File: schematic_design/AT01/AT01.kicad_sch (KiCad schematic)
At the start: 42 parts, among them J1 JST Connector, J2 Conn_01x08_Pin, J3 USB_C_Receptacle_USB2.0, M2 Motor_DC (Pump), M3 Motor_DC (Solenoid), Q1 DMG2301L, Q2 2N7002, Q3 2N7002, SW1 SW_Push, U1 MPRLS0025PA00001A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

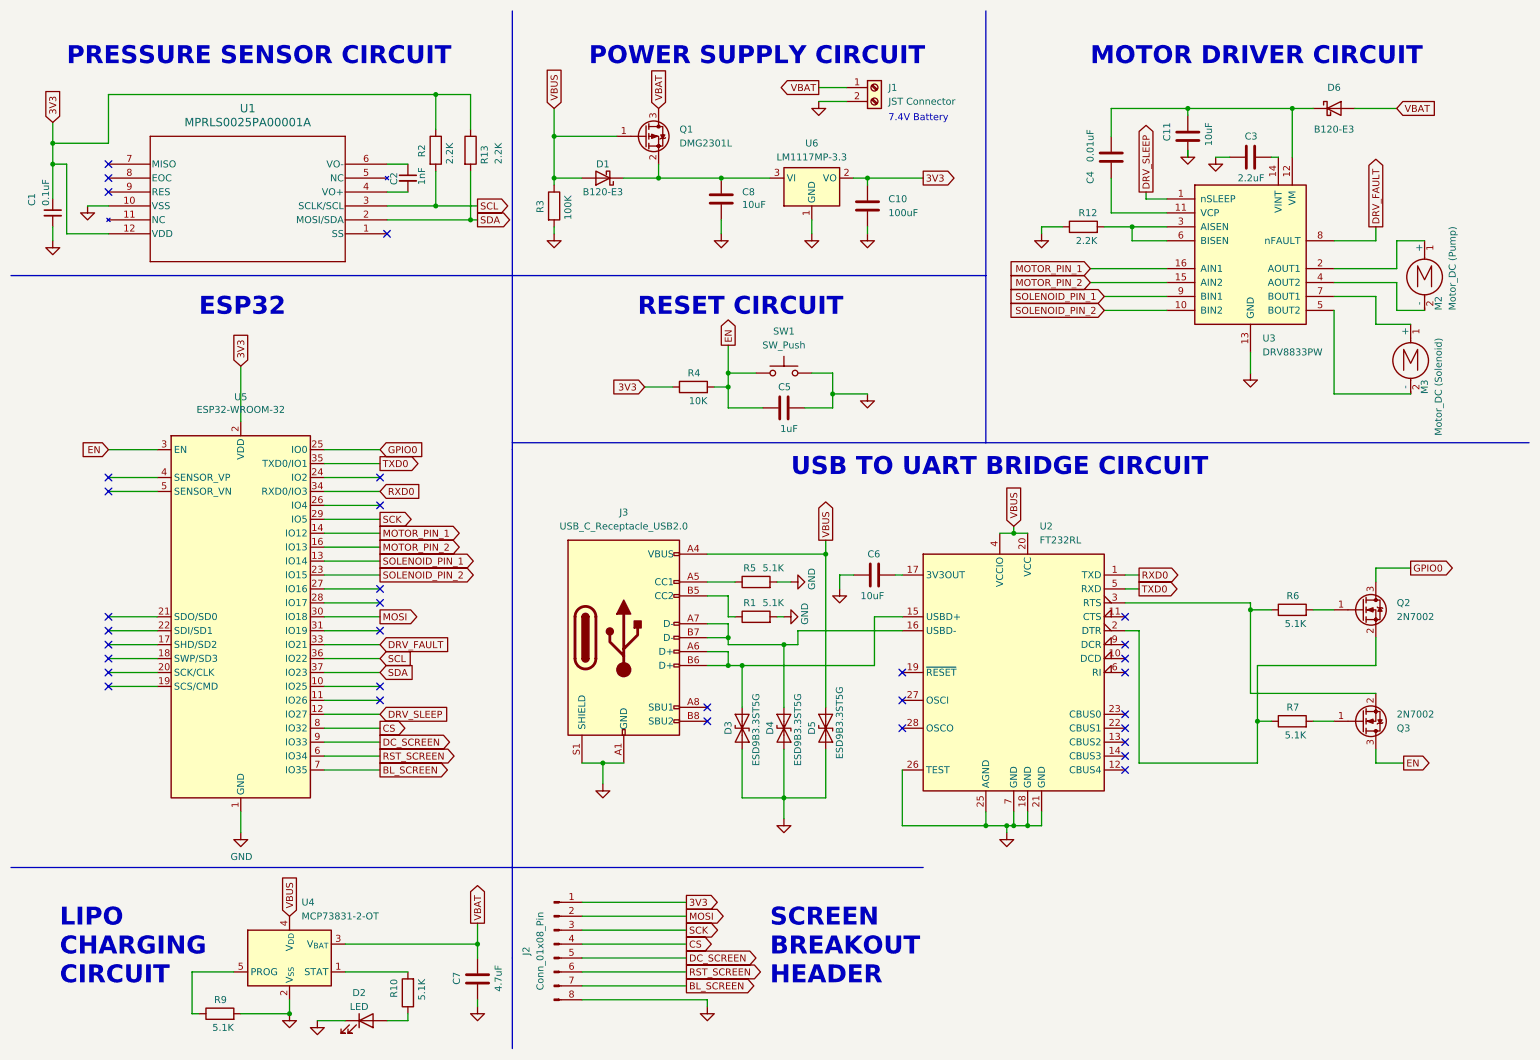
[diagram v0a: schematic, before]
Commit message: reddit fixes, adding buttons/leds, restarting pcb layout
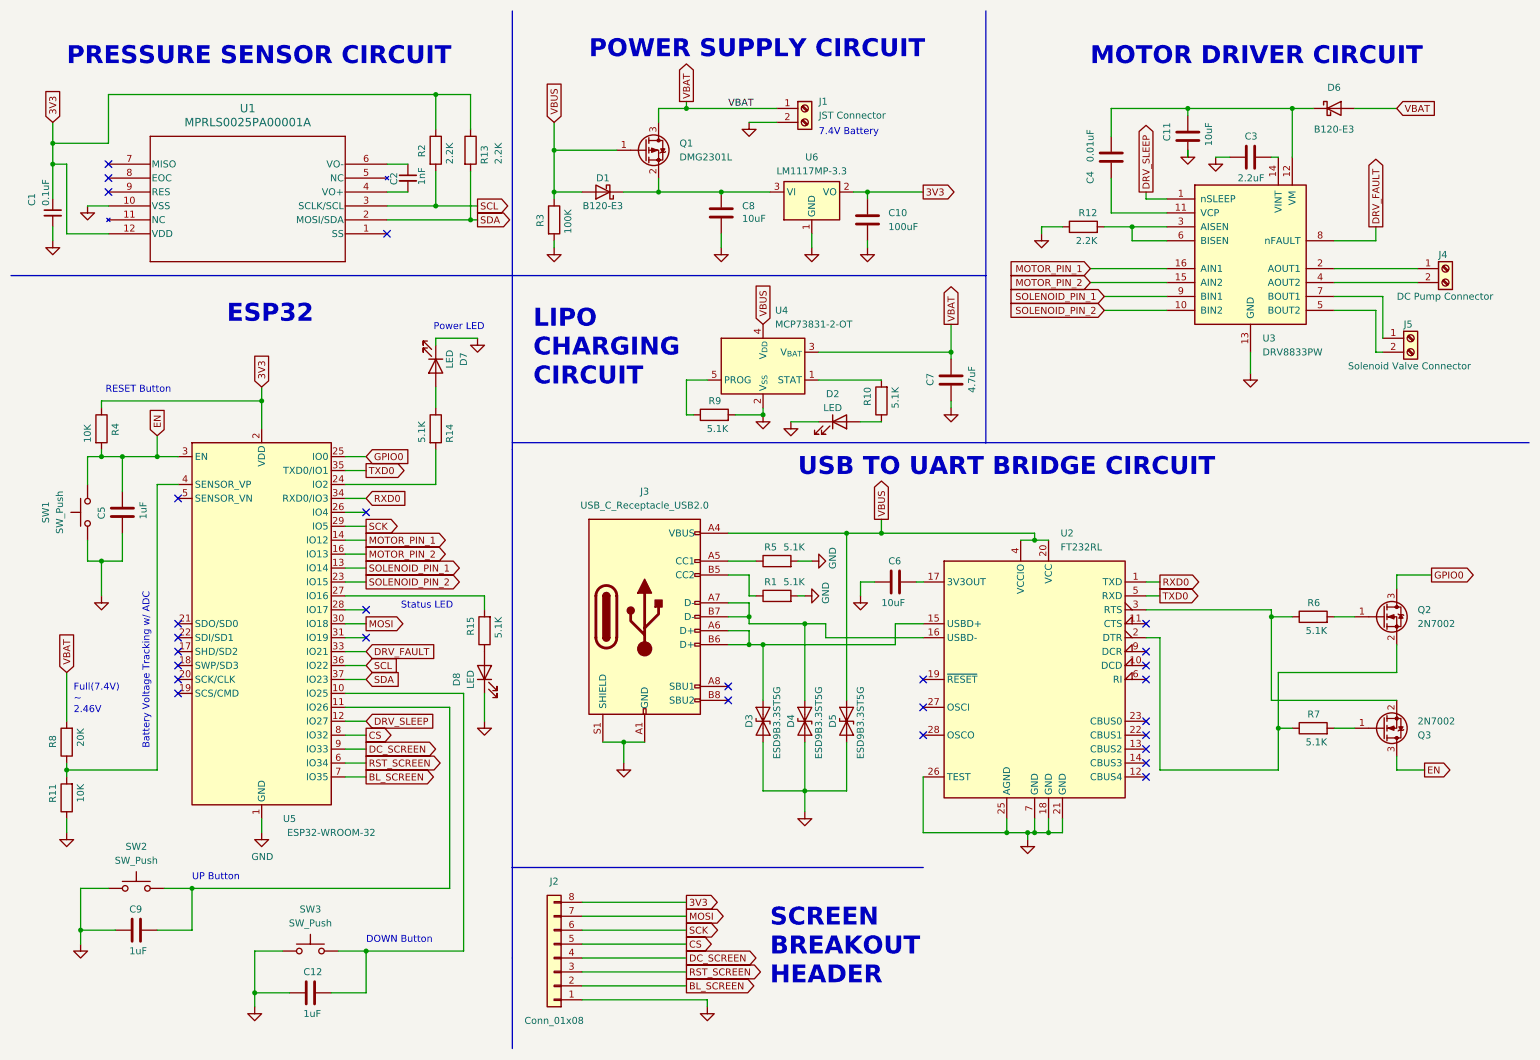
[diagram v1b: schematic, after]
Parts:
- removed J2: Conn_01x08_Pin, Connector_PinHeader_1.00mm:PinHeader_1x08_P1.00mm_Vertical, symbol Connector:Conn_01x08_Pin
- removed M2: Motor_DC (Pump), Connector_Samtec_HPM_THT:Samtec_HPM-02-05-x-S_Straight_1x02_Pitch5.08mm, symbol Motor:Motor_DC
- removed M3: Motor_DC (Solenoid), Connector_Samtec_HPM_THT:Samtec_HPM-02-05-x-S_Straight_1x02_Pitch5.08mm, symbol Motor:Motor_DC
- added C12, C9: 1uF, Capacitor_SMD:C_01005_0402Metric_Pad0.57x0.30mm_HandSolder, symbol Device:C
- added D7, D8: LED, LED_THT:LED_D3.0mm, symbol Device:LED
- added J2: Conn_01x08, Connector_PinHeader_1.00mm:PinHeader_1x08_P1.00mm_Vertical, symbol Connector_Generic:Conn_01x08
- added J4: DC Pump Connector, Connector_JST:JST_EH_S2B-EH_1x02_P2.50mm_Horizontal, symbol Connector:Screw_Terminal_01x02
- added J5: Solenoid Valve Connector, Connector_JST:JST_EH_S2B-EH_1x02_P2.50mm_Horizontal, symbol Connector:Screw_Terminal_01x02
- added R11: 10K, Resistor_SMD:R_0402_1005Metric_Pad0.72x0.64mm_HandSolder, symbol Device:R
- added R14, R15: 5.1K, Resistor_SMD:R_0402_1005Metric_Pad0.72x0.64mm_HandSolder, symbol Device:R
- added R8: 20K, Resistor_SMD:R_0402_1005Metric_Pad0.72x0.64mm_HandSolder, symbol Device:R
- added SW2, SW3: SW_Push, Button_Switch_THT:SW_PUSH_6mm, symbol Switch:SW_Push
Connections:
- net 3V3: now also J2.8 (Pin_8)
- net BL_SCREEN: now also J2.2 (Pin_2)
- net CS: now also J2.5 (Pin_5)
- net DC_SCREEN: now also J2.4 (Pin_4)
- net GND: now also C12.2, C9.2, D7.1 (K), D8.1 (K), J2.1 (Pin_1), R11.1, SW2.2, SW3.2
- net MOSI: now also J2.7 (Pin_7)
- net RST_SCREEN: now also J2.3 (Pin_3)
- net SCK: now also J2.6 (Pin_6)
- net VBAT: now also R8.2
- net at U5.10 (IO25): now also C12.1, SW3.1
- net at U5.11 (IO26): now also C9.1, SW2.1
- net at U5.24 (IO2): now also R14.2
- net at U5.27 (IO16): now also R15.2
- net at U5.4 (SENSOR_VP): now also R11.2, R8.1
- net at U3.2 (AOUT1): now also J4.1 (Pin_1)
- net at U3.4 (AOUT2): now also J4.2 (Pin_2)
- net at U3.5 (BOUT2): now also J5.2 (Pin_2)
- net at U3.7 (BOUT1): now also J5.1 (Pin_1)
- new net: D7.2 (A), R14.1
- new net: D8.2 (A), R15.1
- no-connect marks 33 -> 28
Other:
- note added: "Battery Voltage Tracking w/ ADC"
- note added: "DOWN Button"
- note added: "Full(7.4V) ~ 2.46V"
- note added: "Power LED"
- note added: "RESET Button"
- note added: "Status LED"
- note added: "UP Button"
- note removed: "RESET CIRCUIT"
- title: BP - Initial Revision -> AT01 - Initial Revision
- moved on the sheet: C10, C5, C6, C7, C8, D1, D2, D3, D4, D5, J1, J3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

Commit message: initial layout revision
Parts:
- added C13: 10uF, Capacitor_SMD:C_1206_3216Metric_Pad1.33x1.80mm_HandSolder, symbol Device:C_Polarized_Small_US
- added H1, H2, H3, H4: MountingHole, MountingHole:MountingHole_2.2mm_M2_ISO7380, symbol Mechanical:MountingHole
- C1, C10, C11, C12, C2, C3, C4, C5, C6, C7, C8, C9: footprint Capacitor_SMD:C_01005_0402Metric_Pad0.57x0.30mm_HandSolder -> Capacitor_SMD:C_0402_1005Metric_Pad0.74x0.62mm_HandSolder
- J3: footprint Connector_USB:USB_C_Receptacle_Molex_105450-0101 -> Connector_USB:USB_C_Receptacle_HRO_TYPE-C-31-M-12
- U5: footprint RF_Module:ESP32-WROOM-32D -> RF_Module:ESP32-WROOM-32U; symbol RF_Module:ESP32-WROOM-32D -> RF_Module:ESP32-WROOM-32U
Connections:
- net 3V3: now also C13.1
- net BL_SCREEN: now also J2.3 (Pin_3); no longer J2.2 (Pin_2)
- net CS: now also J2.4 (Pin_4); no longer J2.5 (Pin_5)
- net DC_SCREEN: now also J2.5 (Pin_5); no longer J2.4 (Pin_4)
- net DRV_FAULT: now also U5.12 (IO27); no longer U5.33 (IO21)
- net DRV_SLEEP: now also U5.11 (IO26); no longer U5.12 (IO27)
- net GND: now also C13.2
- net RST_SCREEN: now also J2.2 (Pin_2); no longer J2.3 (Pin_3)
- net at C9.1, SW2.1: now also U5.33 (IO21); no longer U5.11 (IO26)
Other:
- moved on the sheet: C10, C11, R8

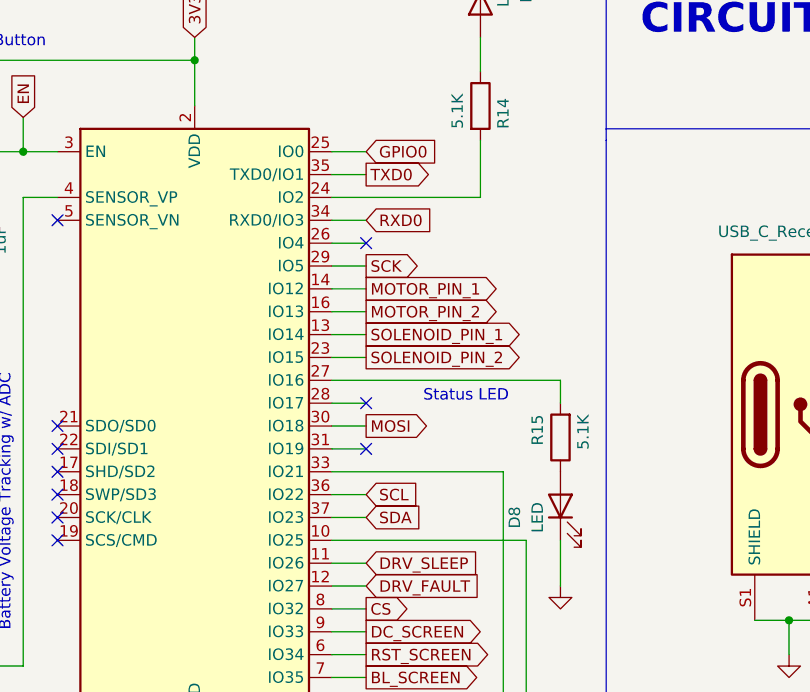
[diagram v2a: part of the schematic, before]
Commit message: updated incorrect UART pins
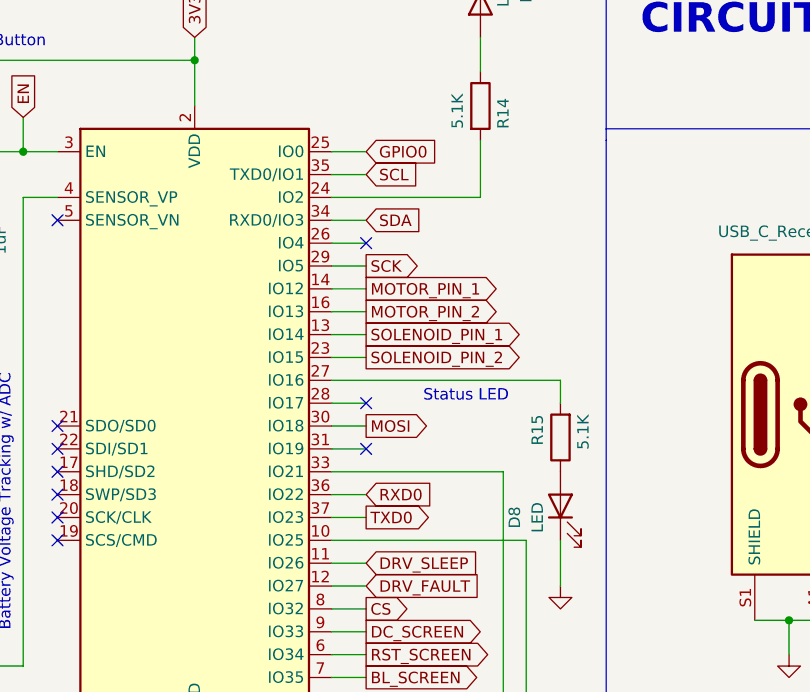
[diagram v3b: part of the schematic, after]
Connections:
- net RXD0: now also U5.36 (IO22); no longer U5.34 (RXD0/IO3)
- net SCL: now also U5.35 (TXD0/IO1); no longer U5.36 (IO22)
- net SDA: now also U5.34 (RXD0/IO3); no longer U5.37 (IO23)
- net TXD0: now also U5.37 (IO23); no longer U5.35 (TXD0/IO1)

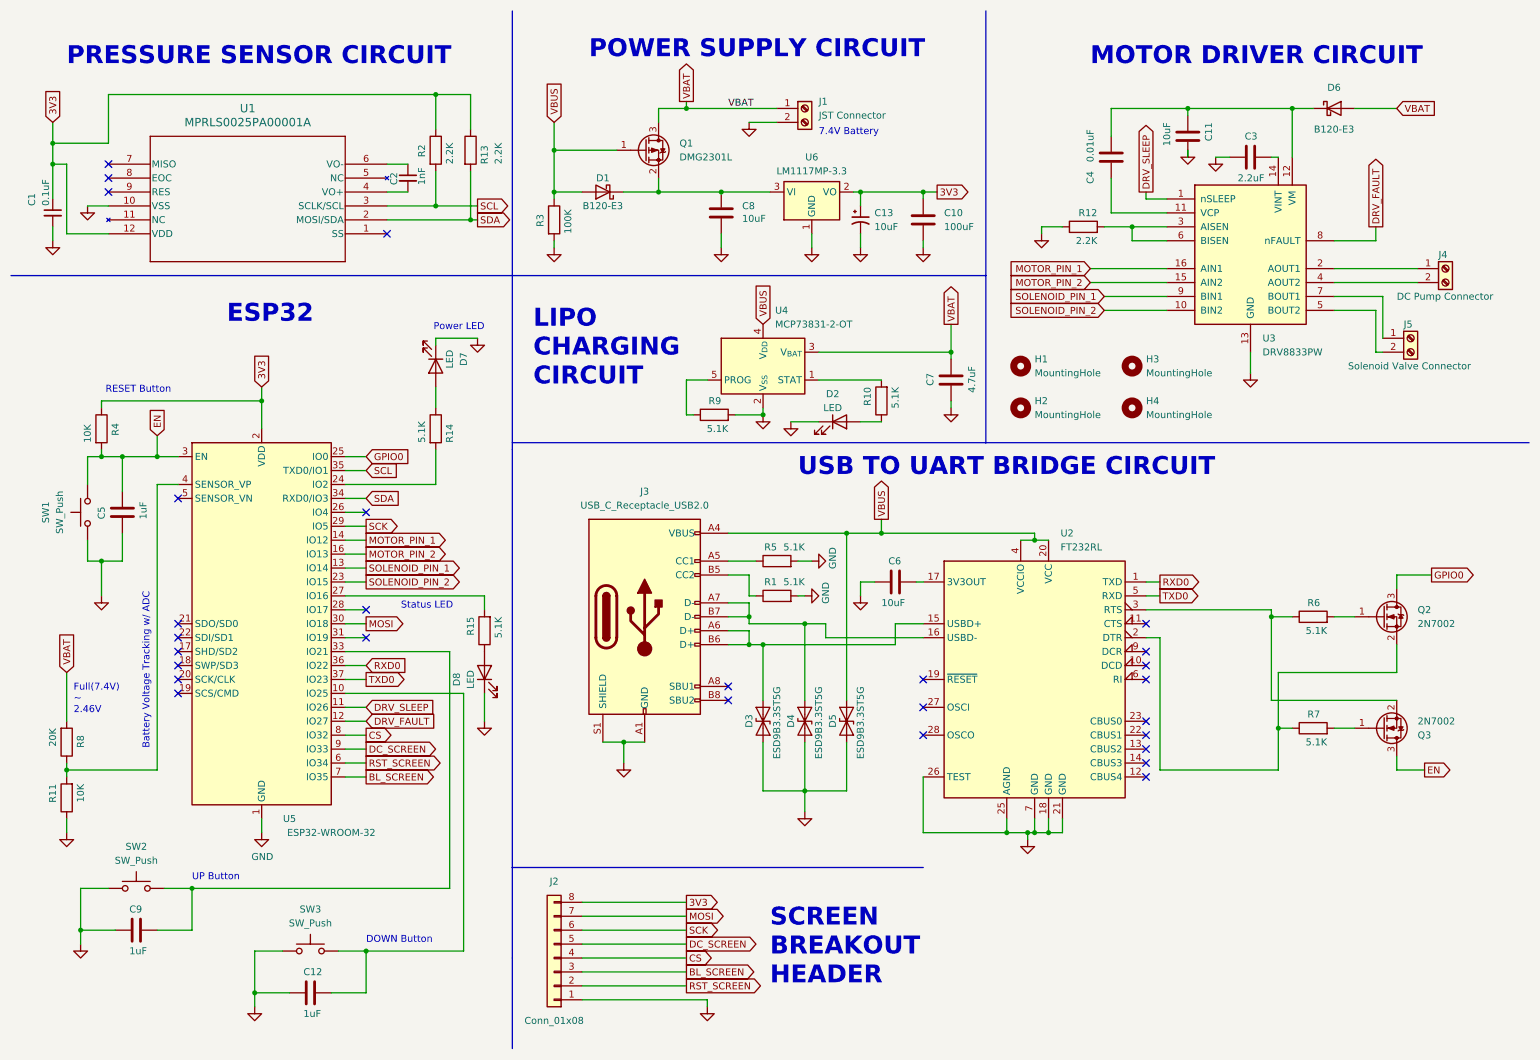
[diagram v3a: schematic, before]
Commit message: moving gnd panel to back copper, button modifications
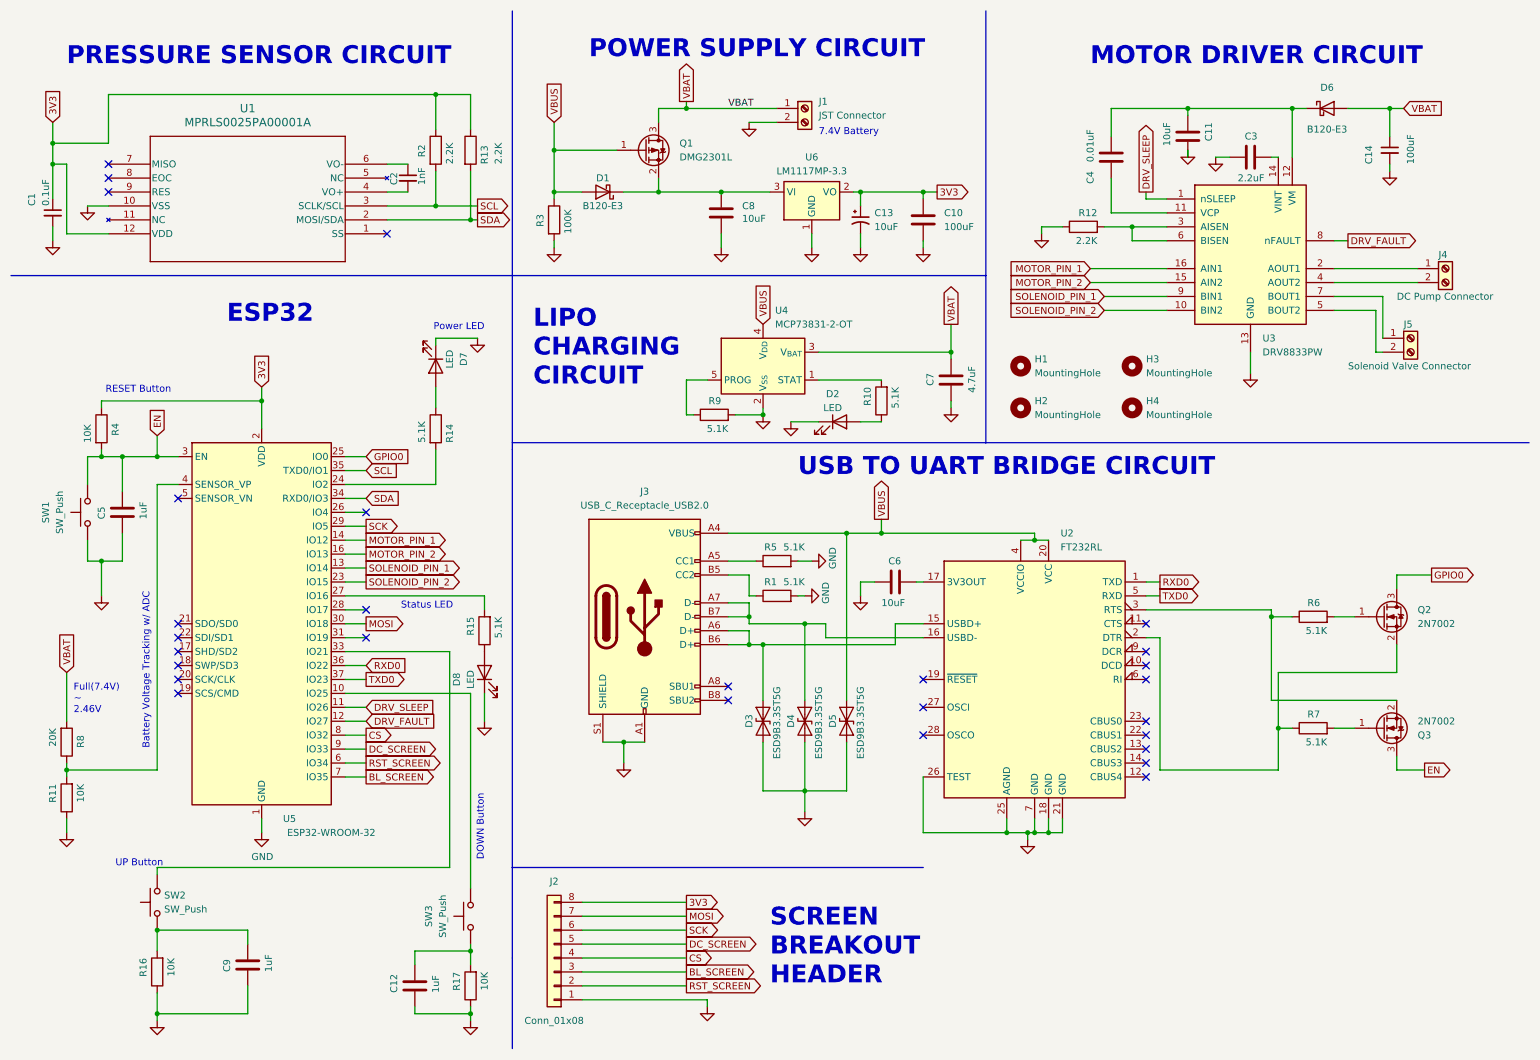
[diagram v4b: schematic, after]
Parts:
- added C14: 100uF, Capacitor_SMD:C_0402_1005Metric_Pad0.74x0.62mm_HandSolder, symbol Device:C_Small
- added R16, R17: 10K, Resistor_SMD:R_0402_1005Metric_Pad0.72x0.64mm_HandSolder, symbol Device:R
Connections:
- net GND: now also C14.2, R16.1, R17.1; no longer SW2.2, SW3.2
- net VBAT: now also C14.1
- net at SW3.1, U5.10 (IO25): no longer C12.1
- net at SW2.1, U5.33 (IO21): no longer C9.1
- new net: C12.1, R17.2, SW3.2
- new net: C9.1, R16.2, SW2.2
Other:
- moved on the sheet: C12, D6, SW2, SW3
